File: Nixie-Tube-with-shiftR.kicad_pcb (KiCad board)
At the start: 2 copper layers, 37 x 44 mm, 55 parts, among them J1 Conn_01x06_Male, J2 Conn_01x01_Female, J3 Conn_01x06_Female, J4 Conn_01x01_Male, Q1 MMBTA42LT1, Q10 MMBTA42LT1, Q11 AO3400, Q12 AO3400, Q13 AO3400, Q14 MMBTA42LT1, Q15 MMBTA42LT1, Q2 MMBTA42LT1, Q3 MMBTA42LT1, Q4 MMBTA42LT1, Q5 MMBTA42LT1, Q6 MMBTA42LT1, Q7 MMBTA42LT1, Q8 MMBTA42LT1, Q9 MMBTA42LT1, U1 74HC595D, U2 nixie-tube, U3 74HC595D, U4 ams1117-5.0

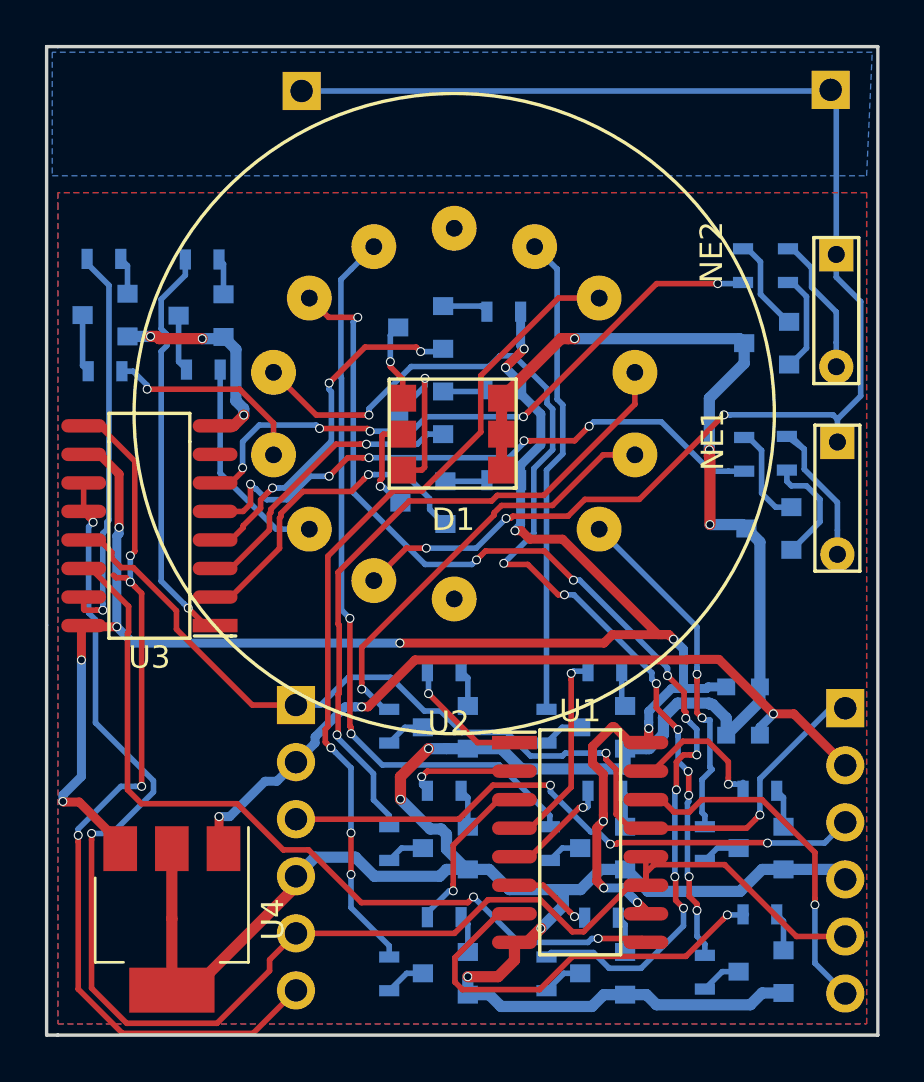
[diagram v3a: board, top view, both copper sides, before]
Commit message: fixed pin headers placement not the same with power supply
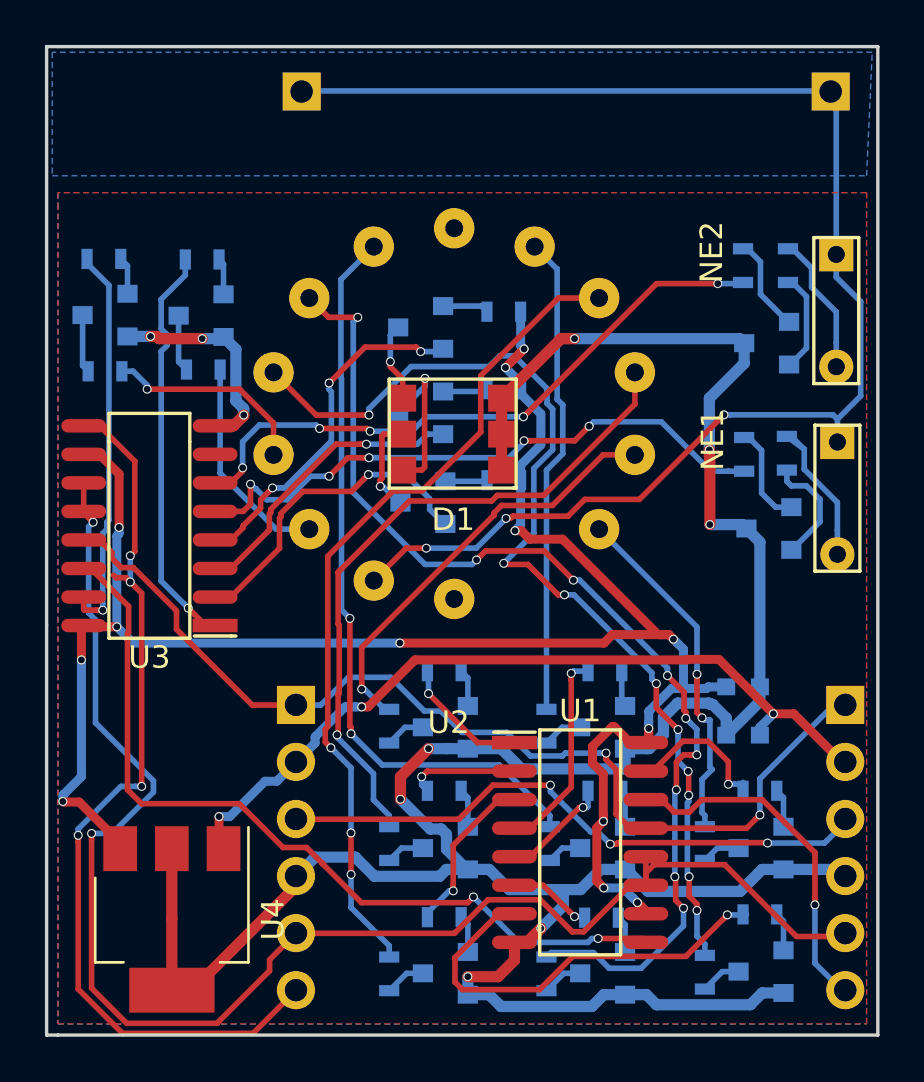
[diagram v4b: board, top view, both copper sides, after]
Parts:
- moved J3 0.15 mm to (187.1, 73.3)
- moved J2 0.08 mm to (186.4, 46.0)
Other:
- board text added: "2mm pin to bottom"
- board text added: "2mm pin to top"
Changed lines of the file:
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@@
   (general
     (links 106)
-    (no_connects 1)
-    (area 151.424999 43.924999 188.575001 88.075001)
+    (no_connects 0)
+    (area 149.233333 42.175 199.225239 91.35)
     (thickness 1.6)
-    (drawings 9)
-    (tracks 886)
+    (drawings 11)
+    (tracks 888)
     (zones 0)
     (modules 55)
@@
   )
   (module Socket_Strips:Socket_Strip_Angled_1x06_Pitch2.54mm (layer B.Cu)
-    (at 187.05 73.45 180)
+    (at 187.05 73.3 180)
     (descr "Through hole angled socket strip, 1x06, 2.54mm pitch, 8.51mm socket length, single row")
     (tags "Through hole angled socket strip THT 1x06 2.54mm single row")
@@
   )
   (module Pin_Headers:Pin_Header_Angled_1x06_Pitch2.54mm (layer B.Cu)
-    (at 162.6 73.31 180)
+    (at 162.6 73.3 180)
     (descr "Through hole angled pin header, 1x06, 2.54mm pitch, 6mm pin length, single row")
     (tags "Through hole angled pin header THT 1x06 2.54mm single row")
@@
   )
   (module Pin_Headers:Pin_Header_Angled_1x01_Pitch2.54mm (layer B.Cu)
-    (at 162.85 45.975 180)
+    (at 162.85 46 180)
     (descr "Through hole angled pin header, 1x01, 2.54mm pitch, 6mm pin length, single row")
     (tags "Through hole angled pin header THT 1x01 2.54mm single row")
@@
   )
   (module Socket_Strips:Socket_Strip_Angled_1x01_Pitch2.54mm (layer B.Cu)
-    (at 186.4 45.925 180)
+    (at 186.4 46 180)
     (descr "Through hole angled socket strip, 1x01, 2.54mm pitch, 8.51mm socket length, single row")
     (tags "Through hole angled socket strip THT 1x01 2.54mm single row")
@@
       (effects (font (size 1 1) (thickness 0.15)))
     )
-    (fp_circle (center 0 0) (end 14.25 0) (layer F.SilkS) (width 0.15))
-    (pad ic thru_hole circle (at 0 -8.25 77.1429) (size 2 2) (drill 0.75) (layers *.Cu *.Mask)
+    (fp_circle (center 0 0) (end 14.25 0) (layer F.CrtYd) (width 0.15))
+    (pad ic thru_hole circle (at 0 -8.25 77.1429) (size 1.8 1.8) (drill 0.8) (layers *.Cu *.Mask)
       (net 68 "Net-(U2-Padic)"))
-    (pad 6 thru_hole circle (at -3.579541 -7.432993 77.1429) (size 2 2) (drill 0.75) (layers *.Cu *.Mask)
+    (pad 6 thru_hole circle (at -3.579541 -7.432993 77.1429) (size 1.8 1.8) (drill 0.8) (layers *.Cu *.Mask)
       (net 44 "Net-(R5-Pad1)"))
-    (pad 7 thru_hole circle (at -6.45011 -5.143791 77.1429) (size 2 2) (drill 0.75) (layers *.Cu *.Mask)
+    (pad 7 thru_hole circle (at -6.45011 -5.143791 77.1429) (size 1.8 1.8) (drill 0.8) (layers *.Cu *.Mask)
       (net 43 "Net-(R4-Pad1)"))
-    (pad 8 thru_hole circle (at -8.043155 -1.835798 77.1429) (size 2 2) (drill 0.75) (layers *.Cu *.Mask)
+    (pad 8 thru_hole circle (at -8.043155 -1.835798 77.1429) (size 1.8 1.8) (drill 0.8) (layers *.Cu *.Mask)
       (net 42 "Net-(R3-Pad1)"))
-    (pad 9 thru_hole circle (at -8.043155 1.835798 77.1429) (size 2 2) (drill 0.75) (layers *.Cu *.Mask)
+    (pad 9 thru_hole circle (at -8.043155 1.835798 77.1429) (size 1.8 1.8) (drill 0.8) (layers *.Cu *.Mask)
       (net 41 "Net-(R2-Pad1)"))
-    (pad 0 thru_hole circle (at -6.45011 5.143791 77.1429) (size 2 2) (drill 0.75) (layers *.Cu *.Mask)
+    (pad 0 thru_hole circle (at -6.45011 5.143791 77.1429) (size 1.8 1.8) (drill 0.8) (layers *.Cu *.Mask)
       (net 40 "Net-(R1-Pad1)"))
-    (pad A thru_hole circle (at -3.579541 7.432993 77.1429) (size 2 2) (drill 0.75) (layers *.Cu *.Mask)
+    (pad A thru_hole circle (at -3.579541 7.432993 77.1429) (size 1.8 1.8) (drill 0.8) (layers *.Cu *.Mask)
       (net 10 "Net-(J2-Pad1)"))
-    (pad NC thru_hole circle (at 0 8.25 77.1429) (size 2 2) (drill 0.75) (layers *.Cu *.Mask)
+    (pad NC thru_hole circle (at 0 8.25 77.1429) (size 1.8 1.8) (drill 0.8) (layers *.Cu *.Mask)
       (net 69 "Net-(U2-PadNC)"))
-    (pad 1 thru_hole circle (at 6.45011 5.143791 77.1429) (size 2 2) (drill 0.75) (layers *.Cu *.Mask)
+    (pad 1 thru_hole circle (at 6.45011 5.143791 77.1429) (size 1.8 1.8) (drill 0.8) (layers *.Cu *.Mask)
       (net 49 "Net-(R10-Pad1)"))
-    (pad 2 thru_hole circle (at 8.043155 1.835798 77.1429) (size 2 2) (drill 0.75) (layers *.Cu *.Mask)
+    (pad 2 thru_hole circle (at 8.043155 1.835798 77.1429) (size 1.8 1.8) (drill 0.8) (layers *.Cu *.Mask)
       (net 48 "Net-(R9-Pad1)"))
-    (pad 3 thru_hole circle (at 8.043155 -1.835798 77.1429) (size 2 2) (drill 0.75) (layers *.Cu *.Mask)
+    (pad 3 thru_hole circle (at 8.043155 -1.835798 77.1429) (size 1.8 1.8) (drill 0.8) (layers *.Cu *.Mask)
       (net 47 "Net-(R8-Pad1)"))
-    (pad 4 thru_hole circle (at 6.45011 -5.143791 77.1429) (size 2 2) (drill 0.75) (layers *.Cu *.Mask)
+    (pad 4 thru_hole circle (at 6.45011 -5.143791 77.1429) (size 1.8 1.8) (drill 0.8) (layers *.Cu *.Mask)
       (net 46 "Net-(R7-Pad1)"))
-    (pad 5 thru_hole circle (at 3.579541 -7.432993 77.1429) (size 2 2) (drill 0.75) (layers *.Cu *.Mask)
+    (pad 5 thru_hole circle (at 3.579541 -7.432993 77.1429) (size 1.8 1.8) (drill 0.8) (layers *.Cu *.Mask)
       (net 45 "Net-(R6-Pad1)"))
   )
+  (gr_text "2mm\npin to top" (at 186.75 43) (layer Eco1.User)
+    (effects (font (size 0.5 0.5) (thickness 0.1)))
+  )
+  (gr_text "2mm\n pin to bottom" (at 187.25 89.25) (layer Eco1.User)
+    (effects (font (size 0.5 0.5) (thickness 0.1)))
+  )
   (gr_line (start 151.5 44) (end 152 44) (layer Edge.Cuts) (width 0.15))
   (gr_line (start 151.5 69.75) (end 151.5 44) (layer Edge.Cuts) (width 0.15))
@@
   (segment (start 175.216379 77.868621) (end 175.378237 77.868621) (width 0.25) (layer F.Cu) (net 59))
   (segment (start 175.5 77.025) (end 175.6 77.125) (width 0.25) (layer B.Cu) (net 59) (status 30))
+  (segment (start 170.5 81.85) (end 170.244999 82.105001) (width 0.25) (layer F.Cu) (net 60))
+  (segment (start 170.244999 82.105001) (end 165.514003 82.105001) (width 0.25) (layer F.Cu) (net 60))
+  (segment (start 165.514003 82.105001) (end 163.775001 80.365999) (width 0.25) (layer F.Cu) (net 60))
+  (segment (start 163.775001 80.365999) (end 163.775001 80.355999) (width 0.25) (layer F.Cu) (net 60))
+  (segment (start 163.069002 79.65) (end 162.025 79.65) (width 0.25) (layer F.Cu) (net 60))
+  (segment (start 155.1 77.075) (end 155.1 70.127002) (width 0.25) (layer F.Cu) (net 60))
+  (segment (start 163.775001 80.355999) (end 163.069002 79.65) (width 0.25) (layer F.Cu) (net 60))
+  (segment (start 160.074999 77.699999) (end 155.724999 77.699999) (width 0.25) (layer F.Cu) (net 60))
+  (segment (start 162.025 79.65) (end 160.074999 77.699999) (width 0.25) (layer F.Cu) (net 60))
+  (segment (start 155.724999 77.699999) (end 155.1 77.075) (width 0.25) (layer F.Cu) (net 60))
+  (segment (start 155.1 70.127002) (end 155.150001 70.077001) (width 0.25) (layer F.Cu) (net 60))
+  (segment (start 153.463897 67.23) (end 153.15 67.23) (width 0.25) (layer F.Cu) (net 60))
+  (segment (start 155.150001 70.077001) (end 155.150001 68.916104) (width 0.25) (layer F.Cu) (net 60))
+  (segment (start 155.150001 68.916104) (end 153.463897 67.23) (width 0.25) (layer F.Cu) (net 60))
   (segment (start 175.592169 83.874989) (end 175.767158 83.7) (width 0.25) (layer B.Cu) (net 60))
   (segment (start 172.524989 83.874989) (end 175.592169 83.874989) (width 0.25) (layer B.Cu) (net 60))
   (segment (start 170.5 81.85) (end 172.524989 83.874989) (width 0.25) (layer B.Cu) (net 60))
   (segment (start 175.767158 83.7) (end 176.05 83.7) (width 0.25) (layer B.Cu) (net 60))
-  (segment (start 153.463897 67.23) (end 153.15 67.23) (width 0.25) (layer F.Cu) (net 60))
-  (segment (start 165.514003 82.105001) (end 163.164001 79.754999) (width 0.25) (layer F.Cu) (net 60))
-  (segment (start 155.150001 68.916104) (end 153.463897 67.23) (width 0.25) (layer F.Cu) (net 60))
-  (segment (start 155.150001 70.077001) (end 155.150001 68.916104) (width 0.25) (layer F.Cu) (net 60))
-  (segment (start 155.1 77.075) (end 155.1 70.127002) (width 0.25) (layer F.Cu) (net 60))
-  (segment (start 155.1 70.127002) (end 155.150001 70.077001) (width 0.25) (layer F.Cu) (net 60))
-  (segment (start 155.724999 77.699999) (end 155.1 77.075) (width 0.25) (layer F.Cu) (net 60))
-  (segment (start 159.980999 77.699999) (end 155.724999 77.699999) (width 0.25) (layer F.Cu) (net 60))
-  (segment (start 162.035999 79.754999) (end 159.980999 77.699999) (width 0.25) (layer F.Cu) (net 60))
-  (segment (start 163.164001 79.754999) (end 162.035999 79.754999) (width 0.25) (layer F.Cu) (net 60))
-  (segment (start 170.244999 82.105001) (end 165.514003 82.105001) (width 0.25) (layer F.Cu) (net 60))
-  (segment (start 170.5 81.85) (end 170.244999 82.105001) (width 0.25) (layer F.Cu) (net 60))
   (via (at 170.5 81.85) (size 0.4) (drill 0.3) (layers F.Cu B.Cu) (net 60))
   (segment (start 176.05 83.7) (end 178.005 83.7) (width 0.25) (layer F.Cu) (net 60))

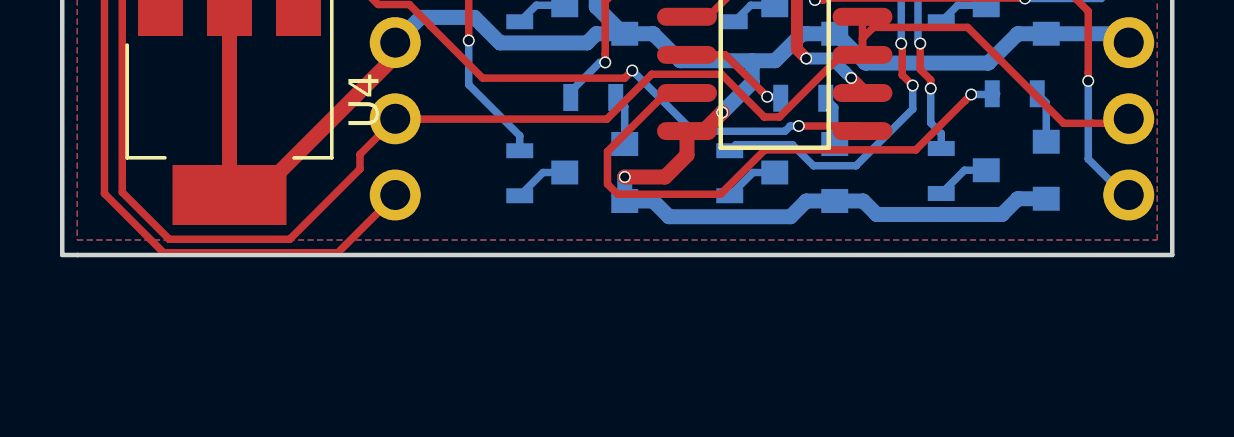
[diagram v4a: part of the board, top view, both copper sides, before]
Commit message: extend board in y dir for placing the 2 headers bottom
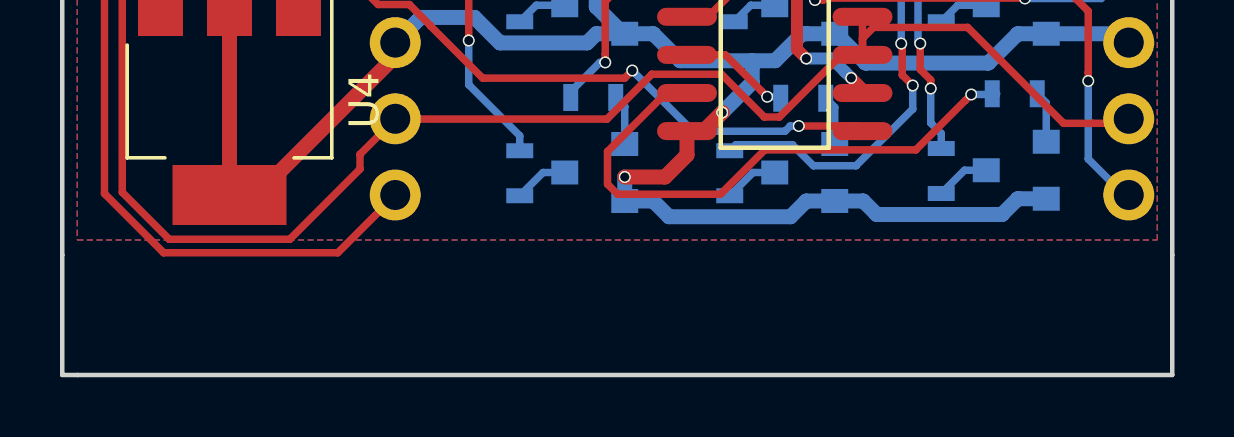
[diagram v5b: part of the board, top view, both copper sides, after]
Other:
- board size 37 x 44 mm -> 37 x 48 mm
- board text added: "37x48mm"
- board text added: "6mm pin to bottom"
- board text removed: "2mm pin to bottom"
- board text removed: "37x44mm"
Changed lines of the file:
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@@
     (links 106)
     (no_connects 0)
-    (area 149.233333 42.175 199.225239 91.35)
+    (area 149.233333 42.175 199.225239 92.075001)
     (thickness 1.6)
-    (drawings 11)
+    (drawings 13)
     (tracks 888)
     (zones 0)
@@
       (net 45 "Net-(R6-Pad1)"))
   )
+  (gr_line (start 188.5 92) (end 188.5 88) (layer Edge.Cuts) (width 0.15))
+  (gr_line (start 151.5 88) (end 151.5 92) (layer Edge.Cuts) (width 0.15))
   (gr_text "2mm\npin to top" (at 186.75 43) (layer Eco1.User)
     (effects (font (size 0.5 0.5) (thickness 0.1)))
   )
-  (gr_text "2mm\n pin to bottom" (at 187.25 89.25) (layer Eco1.User)
+  (gr_text "6mm\n pin to bottom" (at 187.25 89.25) (layer Eco1.User)
     (effects (font (size 0.5 0.5) (thickness 0.1)))
   )
   (gr_line (start 151.5 44) (end 152 44) (layer Edge.Cuts) (width 0.15))
   (gr_line (start 151.5 69.75) (end 151.5 44) (layer Edge.Cuts) (width 0.15))
-  (gr_line (start 151.5 88) (end 152 88) (layer Edge.Cuts) (width 0.15))
+  (gr_line (start 151.5 92) (end 152 92) (layer Edge.Cuts) (width 0.15))
   (gr_line (start 151.5 69.75) (end 151.5 88) (layer Edge.Cuts) (width 0.15))
   (gr_line (start 188.5 44) (end 188.5 88) (layer Edge.Cuts) (width 0.15))
   (gr_line (start 152 44) (end 188.5 44) (layer Edge.Cuts) (width 0.15))
-  (gr_line (start 152 88) (end 188.5 88) (layer Edge.Cuts) (width 0.15))
+  (gr_line (start 152 92) (end 188.5 92) (layer Edge.Cuts) (width 0.15))
   (gr_line (start 188.5 47.625) (end 188.475 47.625) (layer Eco1.User) (width 0.2))
-  (gr_text 37x44mm (at 170.25 90) (layer Eco1.User)
+  (gr_text 37x48mm (at 170.25 90) (layer Eco1.User)
     (effects (font (size 1.5 1.5) (thickness 0.3)))
   )

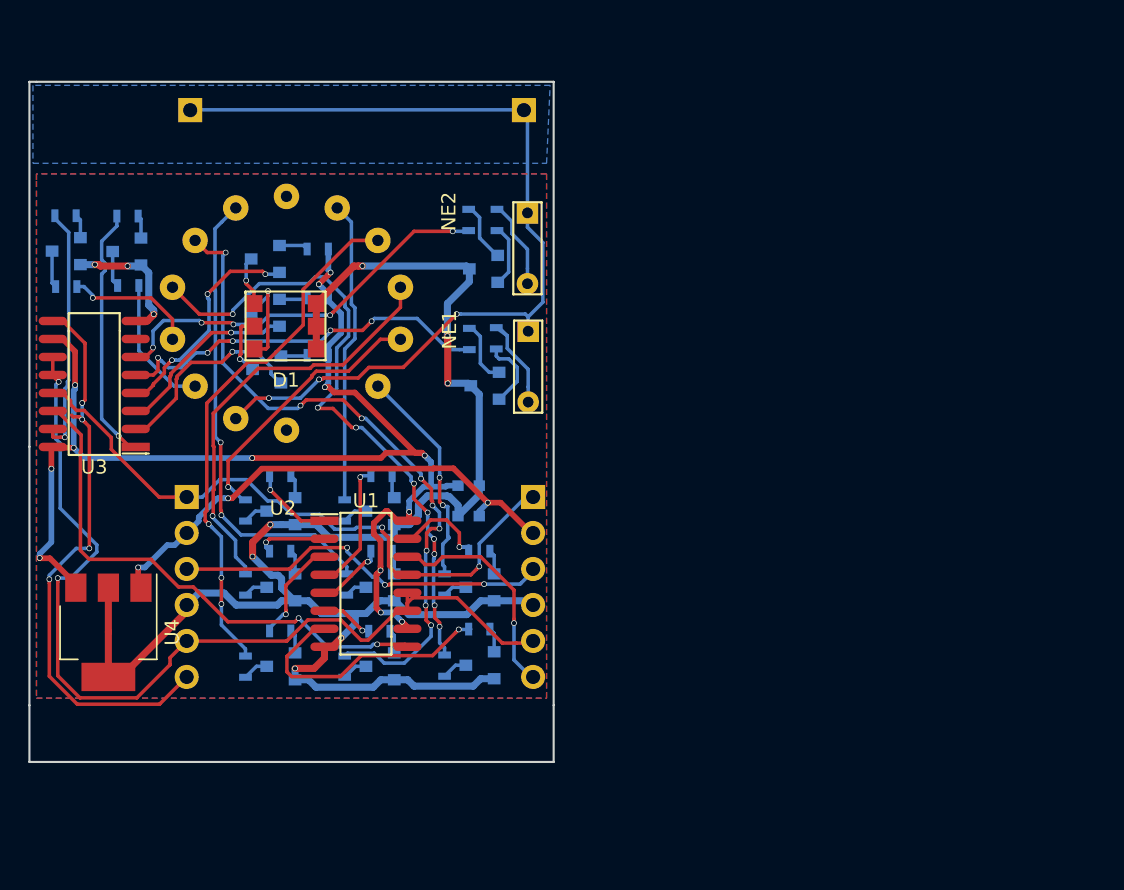
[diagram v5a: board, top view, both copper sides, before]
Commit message: adjust board layout to fit with 7mm pin
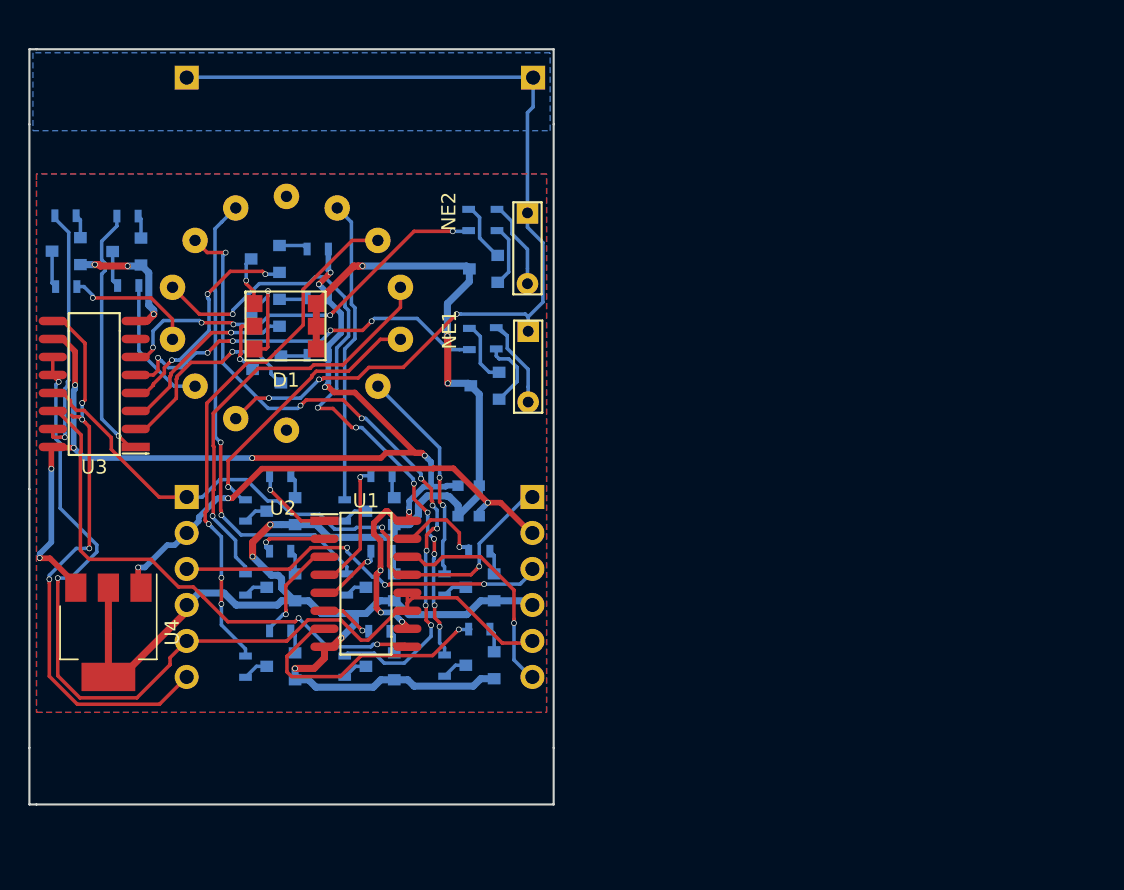
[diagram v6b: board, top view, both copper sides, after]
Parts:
- moved J2 2.39 mm to (187.1, 43.7)
- moved J4 2.31 mm to (162.6, 43.7)
- moved J3 0.05 mm to (187.0, 73.3)
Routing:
- net Net-(J2-Pad1): track 64.0 -> 66.6 mm
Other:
- board size 37 x 48 mm -> 37 x 53.3 mm
- board text removed: "37x48mm"
